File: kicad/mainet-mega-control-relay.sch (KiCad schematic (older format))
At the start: 0 parts

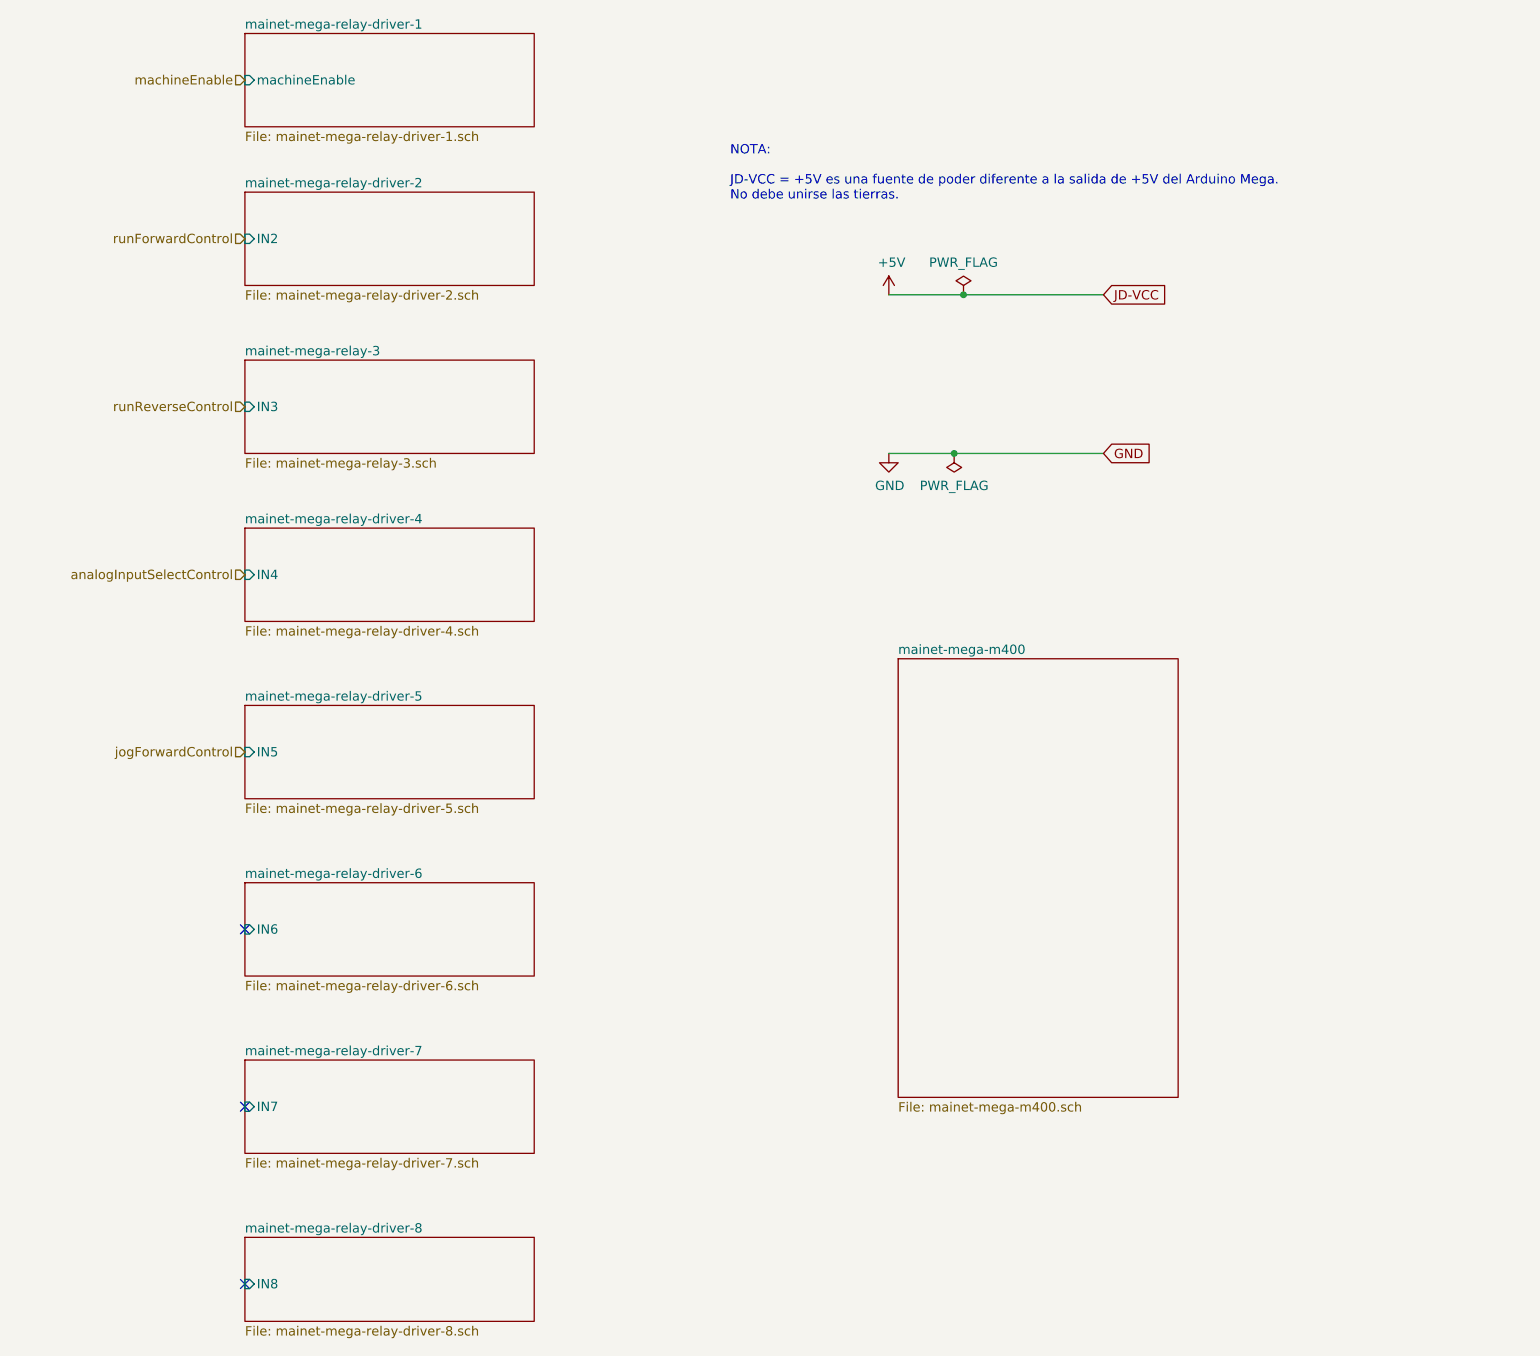
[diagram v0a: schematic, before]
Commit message: Kicad: Modificaciones menores esquemáticos
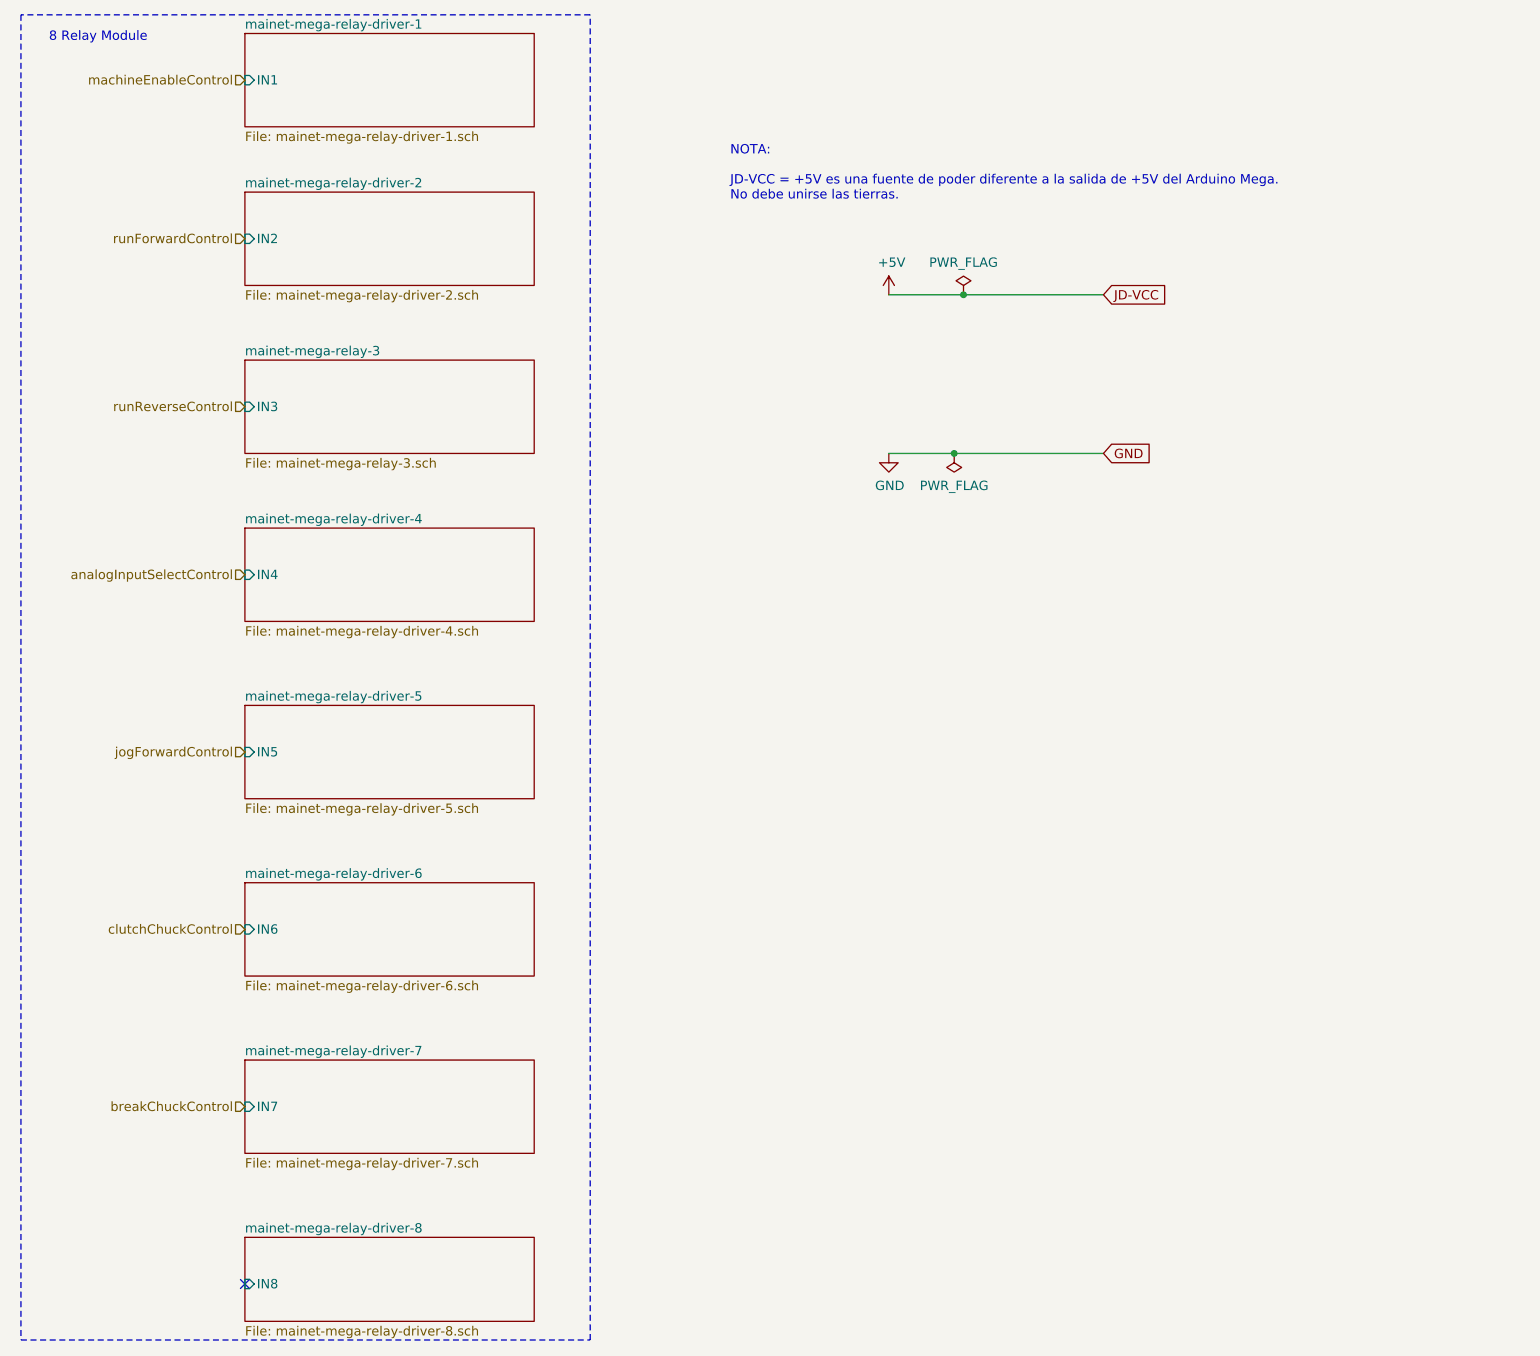
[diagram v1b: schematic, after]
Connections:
- no-connect marks 3 -> 1
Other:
- note added: "8 Relay Module"
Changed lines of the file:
@@
 $Descr A4 11693 8268
 encoding utf-8
-Sheet 5 17
+Sheet 7 17
 Title ""
 Date ""
@@
 F0 "mainet-mega-relay-driver-1" 50
 F1 "mainet-mega-relay-driver-1.sch" 50
-F2 "machineEnable" I L 4950 900 50
+F2 "IN1" I L 4950 900 50
 $EndSheet
 $Sheet
@@
 runReverseControl
 Text HLabel 4950 900  0    50   Input ~ 0
-machineEnable
+machineEnableControl
 Text HLabel 4950 4500 0    50   Input ~ 0
 jogForwardControl
 Text HLabel 4950 3550 0    50   Input ~ 0
 analogInputSelectControl
-NoConn ~ 4950 6400
 NoConn ~ 4950 7350
 Text Notes 7550 1550 0    50   ~ 0
 NOTA:\n\nJD-VCC = +5V es una fuente de poder diferente a la salida de +5V del Arduino Mega.\nNo debe unirse las tierras.
-NoConn ~ 4950 5450
-$Sheet
-S 8450 4000 1500 2350
-U 5FF5E17E
-F0 "mainet-mega-m400" 50
-F1 "mainet-mega-m400.sch" 50
-$EndSheet
+Wire Notes Line
+	3750 550  3750 7650
+Wire Notes Line
+	3750 7650 6800 7650
+Wire Notes Line
+	6800 7650 6800 550
+Wire Notes Line
+	6800 550  3750 550
+Text Notes 3900 700  0    50   ~ 0
+8 Relay Module
+Text HLabel 4950 5450 0    50   Input ~ 0
+clutchChuckControl
+Text HLabel 4950 6400 0    50   Input ~ 0
+breakChuckControl
 $EndSCHEMATC

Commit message: KICAD: Cambio etiqueta breakChuck a brakeChuck y correción del pin
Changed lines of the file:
@@
 clutchChuckControl
 Text HLabel 4950 6400 0    50   Input ~ 0
-breakChuckControl
+brakeChuckControl
 $EndSCHEMATC

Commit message: KICAD: Actualización de esquematicos del módulo de 8 relés de control
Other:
- note added: "D15"
- note added: "D16"
- note added: "D17"
- note added: "D18"
- note added: "D19"
- note added: "D20"
- note added: "D21"
- note added: "NOTA:\n\nJD-VCC = +5V es una fuente de poder diferente a la salida de +5V del Arduino Mega.\nVCC = +5V es la salida de 5V del Arduino Mega\nGND = 0V de la fuente externa de alimentación de los relés. No es la tierra del Arduino.\nNo debe unirse las tierras."
- note removed: "NOTA:\n\nJD-VCC = +5V es una fuente de poder diferente a la salida de +5V del Arduino Mega.\nNo debe unirse las tierras."
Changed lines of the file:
@@
 EESchema Schematic File Version 4
 LIBS:mainet-mega-cache
-LIBS:mainet-mega-5V-to-mp-10v-cache
 EELAYER 30 0
 EELAYER END
@@
 NoConn ~ 4950 7350
 Text Notes 7550 1550 0    50   ~ 0
-NOTA:\n\nJD-VCC = +5V es una fuente de poder diferente a la salida de +5V del Arduino Mega.\nNo debe unirse las tierras.
+NOTA:\n\nJD-VCC = +5V es una fuente de poder diferente a la salida de +5V del Arduino Mega.\nVCC = +5V es la salida de 5V del Arduino Mega\nGND = 0V de la fuente externa de alimentación de los relés. No es la tierra del Arduino.\nNo debe unirse las tierras.
 Wire Notes Line
 	3750 550  3750 7650
@@
 Text HLabel 4950 6400 0    50   Input ~ 0
 brakeChuckControl
+Text Notes 4050 850  0    50   ~ 0
+D21
+Text Notes 4200 1700 0    50   ~ 0
+D20
+Text Notes 4200 2600 0    50   ~ 0
+D19
+Text Notes 3950 3500 0    50   ~ 0
+D18
+Text Notes 4200 4450 0    50   ~ 0
+D17
+Text Notes 4150 5400 0    50   ~ 0
+D16
+Text Notes 4200 6350 0    50   ~ 0
+D15
 $EndSCHEMATC
